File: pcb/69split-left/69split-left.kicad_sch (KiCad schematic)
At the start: 0 parts

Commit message: Finished design and layout?
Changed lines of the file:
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@@
 	(bus
 		(pts
-			(xy 134.62 99.06) (xy 134.62 127)
+			(xy 135.89 99.06) (xy 135.89 127)
 		)
 		(stroke
@@
 	(bus
 		(pts
-			(xy 124.46 127) (xy 134.62 127)
+			(xy 124.46 127) (xy 135.89 127)
 		)
 		(stroke
@@
 	(bus
 		(pts
-			(xy 134.62 99.06) (xy 142.24 99.06)
+			(xy 135.89 99.06) (xy 142.24 99.06)
 		)
 		(stroke

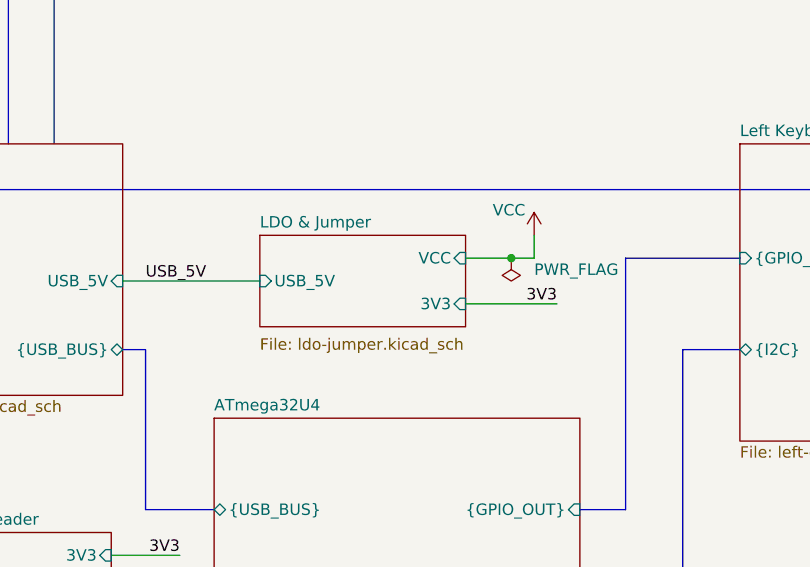
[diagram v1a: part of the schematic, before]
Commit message: Added SPDT switch because I do not want to wait for the KiCAD librarians to approve of my SP3T switch, therefore that will be in future work.
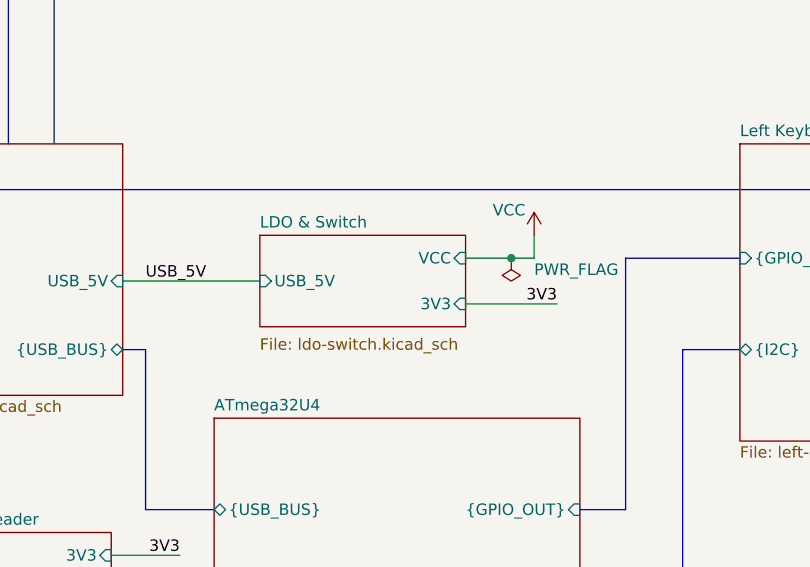
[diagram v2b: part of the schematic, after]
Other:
- sheet LDO & Jumper renamed LDO & Switch
- sheet LDO & Switch: file ldo-jumper.kicad_sch -> ldo-switch.kicad_sch
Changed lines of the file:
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@@
 			(color 0 0 0 0.0000)
 		)
-		(property "Sheetname" "LDO & Jumper"
+		(property "Sheetname" "LDO & Switch"
 			(at 88.9 85.6484 0)
 			(effects
@@
 			)
 		)
-		(property "Sheetfile" "ldo-jumper.kicad_sch"
+		(property "Sheetfile" "ldo-switch.kicad_sch"
 			(at 88.9 97.7396 0)
 			(effects

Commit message: Final touches.
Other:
- note added: "L + R 42mA + 76mA @ 5V 25mA + 51mA @ 3V3 Typical current draw when everythin is in use except the breakout header."
- note removed: "105mA @ 5V 60mA @ 3V3"
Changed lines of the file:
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@@
 		)
 	)
-	(text "105mA @ 5V\n60mA @ 3V3"
-		(exclude_from_sim no)
-		(at 243.84 35.56 0)
+	(text "L + R\n42mA + 76mA @ 5V\n25mA + 51mA @ 3V3\n\nTypical current draw when everythin is in use\nexcept the breakout header."
+		(exclude_from_sim no)
+		(at 209.55 32.766 0)
 		(effects
 			(font
 				(size 2 2)
 			)
-			(justify right)
+			(justify left)
 		)
 	)
@@
 	(text "Keyboard USB-C Connection"
 		(exclude_from_sim no)
-		(at 185.42 55.88 0)
+		(at 184.658 57.15 0)
 		(effects
 			(font
@@
 	)
 	(junction
-		(at 116.84 88.9)
+		(at 115.57 88.9)
 		(diameter 0)
 		(color 0 0 0 0)
@@
 	(wire
 		(pts
+			(xy 115.57 88.9) (xy 119.38 88.9)
+		)
+		(stroke
+			(width 0)
+			(type default)
+		)
+	)
+	(wire
+		(pts
 			(xy 72.39 121.92) (xy 80.01 121.92)
 		)
@@
 	(bus
 		(pts
-			(xy 124.46 134.62) (xy 142.24 134.62)
+			(xy 124.46 137.16) (xy 142.24 137.16)
+		)
+		(stroke
+			(width 0)
+			(type default)
+		)
+	)
+	(bus
+		(pts
+			(xy 129.54 88.9) (xy 142.24 88.9)
 		)
 		(stroke
@@
 	(wire
 		(pts
-			(xy 116.84 88.9) (xy 119.38 88.9)
-		)
-		(stroke
-			(width 0)
-			(type default)
-		)
-	)
-	(bus
-		(pts
-			(xy 129.54 88.9) (xy 142.24 88.9)
-		)
-		(stroke
-			(width 0)
-			(type default)
+			(xy 119.38 88.9) (xy 119.38 86.36)
+		)
+		(stroke
+			(width 0)
+			(type default)
+		)
+	)
+	(bus
+		(pts
+			(xy 135.89 99.06) (xy 135.89 127)
+		)
+		(stroke
+			(width 0)
+			(type default)
+		)
+	)
+	(bus
+		(pts
+			(xy 124.46 127) (xy 135.89 127)
+		)
+		(stroke
+			(width 0)
+			(type default)
+		)
+	)
+	(bus
+		(pts
+			(xy 124.46 116.84) (xy 129.54 116.84)
+		)
+		(stroke
+			(width 0)
+			(type default)
+		)
+	)
+	(bus
+		(pts
+			(xy 129.54 116.84) (xy 129.54 88.9)
+		)
+		(stroke
+			(width 0)
+			(type default)
+		)
+	)
+	(polyline
+		(pts
+			(xy 243.84 53.34) (xy 243.84 76.2)
+		)
+		(stroke
+			(width 0)
+			(type default)
+			(color 0 0 0 1)
 		)
 	)
 	(wire
 		(pts
-			(xy 119.38 88.9) (xy 119.38 86.36)
-		)
-		(stroke
-			(width 0)
-			(type default)
-		)
-	)
-	(bus
-		(pts
-			(xy 135.89 99.06) (xy 135.89 127)
-		)
-		(stroke
-			(width 0)
-			(type default)
-		)
-	)
-	(bus
-		(pts
-			(xy 124.46 127) (xy 135.89 127)
-		)
-		(stroke
-			(width 0)
-			(type default)
-		)
-	)
-	(bus
-		(pts
-			(xy 124.46 116.84) (xy 129.54 116.84)
-		)
-		(stroke
-			(width 0)
-			(type default)
-		)
-	)
-	(bus
-		(pts
-			(xy 129.54 116.84) (xy 129.54 88.9)
+			(xy 111.76 93.98) (xy 121.92 93.98)
+		)
+		(stroke
+			(width 0)
+			(type default)
+		)
+	)
+	(bus
+		(pts
+			(xy 135.89 99.06) (xy 142.24 99.06)
 		)
 		(stroke
@@
 	(polyline
 		(pts
-			(xy 243.84 53.34) (xy 243.84 76.2)
+			(xy 60.96 53.34) (xy 60.96 76.2)
 		)
 		(stroke
@@
 		)
 	)
+	(bus
+		(pts
+			(xy 73.66 99.06) (xy 76.2 99.06)
+		)
+		(stroke
+			(width 0)
+			(type default)
+		)
+	)
 	(wire
 		(pts
-			(xy 111.76 93.98) (xy 121.92 93.98)
-		)
-		(stroke
-			(width 0)
-			(type default)
-		)
-	)
-	(bus
-		(pts
-			(xy 135.89 99.06) (xy 142.24 99.06)
-		)
-		(stroke
-			(width 0)
-			(type default)
-		)
-	)
-	(polyline
-		(pts
-			(xy 60.96 53.34) (xy 60.96 76.2)
-		)
-		(stroke
-			(width 0)
-			(type default)
-			(color 0 0 0 1)
-		)
-	)
-	(bus
-		(pts
-			(xy 73.66 99.06) (xy 76.2 99.06)
-		)
-		(stroke
-			(width 0)
-			(type default)
-		)
-	)
-	(wire
-		(pts
-			(xy 111.76 88.9) (xy 116.84 88.9)
+			(xy 111.76 88.9) (xy 115.57 88.9)
 		)
 		(stroke
@@
 	(symbol
 		(lib_id "power:PWR_FLAG")
-		(at 116.84 88.9 180)
+		(at 115.57 88.9 180)
 		(unit 1)
 		(exclude_from_sim no)
@@
 		(fields_autoplaced yes)
 		(property "Reference" "#FLG01"
-			(at 116.84 90.805 0)
+			(at 115.57 90.805 0)
 			(effects
 				(font
@@
 		)
 		(property "Value" "PWR_FLAG"
-			(at 119.38 90.1699 0)
+			(at 118.11 90.1699 0)
 			(effects
 				(font
@@
 		)
 		(property "Footprint" ""
-			(at 116.84 88.9 0)
+			(at 115.57 88.9 0)
 			(effects
 				(font
@@
 		)
 		(property "Datasheet" "~"
-			(at 116.84 88.9 0)
+			(at 115.57 88.9 0)
 			(effects
 				(font
@@
 		)
 		(property "Description" "Special symbol for telling ERC where power comes from"
-			(at 116.84 88.9 0)
+			(at 115.57 88.9 0)
 			(effects
 				(font
@@
 		)
 		(pin "{LEFT_MATRIX}" bidirectional
-			(at 124.46 134.62 0)
+			(at 124.46 137.16 0)
 			(effects
 				(font
@@
 			)
 		)
-		(pin "{GPIO_OUT}" input
+		(pin "{GPIO_OUT}" output
 			(at 124.46 116.84 0)
 			(effects
@@
 			)
 		)
-		(pin "{INDICATORS}" input
+		(pin "{INDICATORS}" output
 			(at 83.82 152.4 180)
 			(effects
@@
 			)
 		)
-		(pin "{BREAKOUT_HEADER}" input
+		(pin "{BREAKOUT_HEADER}" bidirectional
 			(at 83.82 127 180)
 			(effects
@@
 	)
 	(sheet
-		(at 142.24 127)
+		(at 142.24 129.54)
 		(size 22.86 15.24)
 		(exclude_from_sim no)
@@
 		)
 		(property "Sheetname" "Left Matrix"
-			(at 142.24 126.2884 0)
+			(at 142.24 128.8284 0)
 			(effects
 				(font
@@
 		)
 		(property "Sheetfile" "left-matrix.kicad_sch"
-			(at 142.24 142.8246 0)
+			(at 142.24 145.3646 0)
 			(effects
 				(font
@@
 		)
 		(pin "{LEFT_MATRIX}" bidirectional
-			(at 142.24 134.62 180)
+			(at 142.24 137.16 180)
 			(effects
 				(font
@@
 			)
 		)
-		(pin "USB_5V" input
+		(pin "USB_5V" output
 			(at 73.66 91.44 0)
 			(effects
@@
 			)
 		)
-		(pin "{BREAKOUT_HEADER}" input
+		(pin "{BREAKOUT_HEADER}" bidirectional
 			(at 72.39 127 0)
 			(effects
@@
 			)
 		)
-		(pin "VCC" input
+		(pin "VCC" output
 			(at 111.76 88.9 0)
 			(effects
@@
 			)
 		)
-		(pin "3V3" input
+		(pin "3V3" output
 			(at 111.76 93.98 0)
 			(effects

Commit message: More final touches fml.
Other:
- sheet ATmega32U4: file atmega32u4.kicad_sch -> 69split-left-sheets/atmega32u4.kicad_sch
- sheet Breakout Header: file breakout-header.kicad_sch -> 69split-left-sheets/breakout-header.kicad_sch
- sheet Indicator LEDs: file indicators.kicad_sch -> 69split-left-sheets/indicators.kicad_sch
- sheet LDO & Switch: file ldo-switch.kicad_sch -> 69split-left-sheets/ldo-switch.kicad_sch
- sheet Left Keyboard Connector: file left-conn.kicad_sch -> 69split-left-sheets/left-conn.kicad_sch
- sheet Left Matrix: file left-matrix.kicad_sch -> 69split-left-sheets/left-matrix.kicad_sch
- sheet USB Connector: file usb-conn.kicad_sch -> 69split-left-sheets/usb-conn.kicad_sch
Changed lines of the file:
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@@
 		(on_board yes)
 		(dnp no)
-		(fields_autoplaced yes)
 		(stroke
 			(width 0.1524)
@@
 			)
 		)
-		(property "Sheetfile" "indicators.kicad_sch"
-			(at 49.53 159.9696 0)
+		(property "Sheetfile" "69split-left-sheets/indicators.kicad_sch"
+			(at 28.448 160.528 0)
 			(effects
 				(font
@@
 		(on_board yes)
 		(dnp no)
+		(fields_autoplaced yes)
 		(stroke
 			(width 0.1524)
@@
 			)
 		)
-		(property "Sheetfile" "left-conn.kicad_sch"
-			(at 142.24 109.728 0)
+		(property "Sheetfile" "69split-left-sheets/left-conn.kicad_sch"
+			(at 142.24 109.8046 0)
 			(effects
 				(font
@@
 			)
 		)
-		(property "Sheetfile" "atmega32u4.kicad_sch"
-			(at 83.82 159.9696 0)
+		(property "Sheetfile" "69split-left-sheets/atmega32u4.kicad_sch"
+			(at 83.82 160.6046 0)
 			(effects
 				(font
@@
 			)
 		)
-		(property "Sheetfile" "left-matrix.kicad_sch"
+		(property "Sheetfile" "69split-left-sheets/left-matrix.kicad_sch"
 			(at 142.24 145.3646 0)
 			(effects
@@
 			)
 		)
-		(property "Sheetfile" "usb-conn.kicad_sch"
-			(at 45.72 104.648 0)
+		(property "Sheetfile" "69split-left-sheets/usb-conn.kicad_sch"
+			(at 29.464 104.394 0)
 			(effects
 				(font
@@
 		(on_board yes)
 		(dnp no)
-		(fields_autoplaced yes)
 		(stroke
 			(width 0.1524)
@@
 			)
 		)
-		(property "Sheetfile" "breakout-header.kicad_sch"
-			(at 49.53 135.2046 0)
+		(property "Sheetfile" "69split-left-sheets/breakout-header.kicad_sch"
+			(at 21.336 135.382 0)
 			(effects
 				(font
@@
 			)
 		)
-		(property "Sheetfile" "ldo-switch.kicad_sch"
-			(at 88.9 97.7396 0)
-			(effects
-				(font
+		(property "Sheetfile" "69split-left-sheets/ldo-switch.kicad_sch"
+			(at 88.9 97.1046 0)
+			(effects
+				(font
